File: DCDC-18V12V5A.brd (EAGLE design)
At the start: 40 x 24 mm, 38 parts, among them Q10 NMOSFET, Q9 NMOSFET, U1 LM3150MHX/NOPB

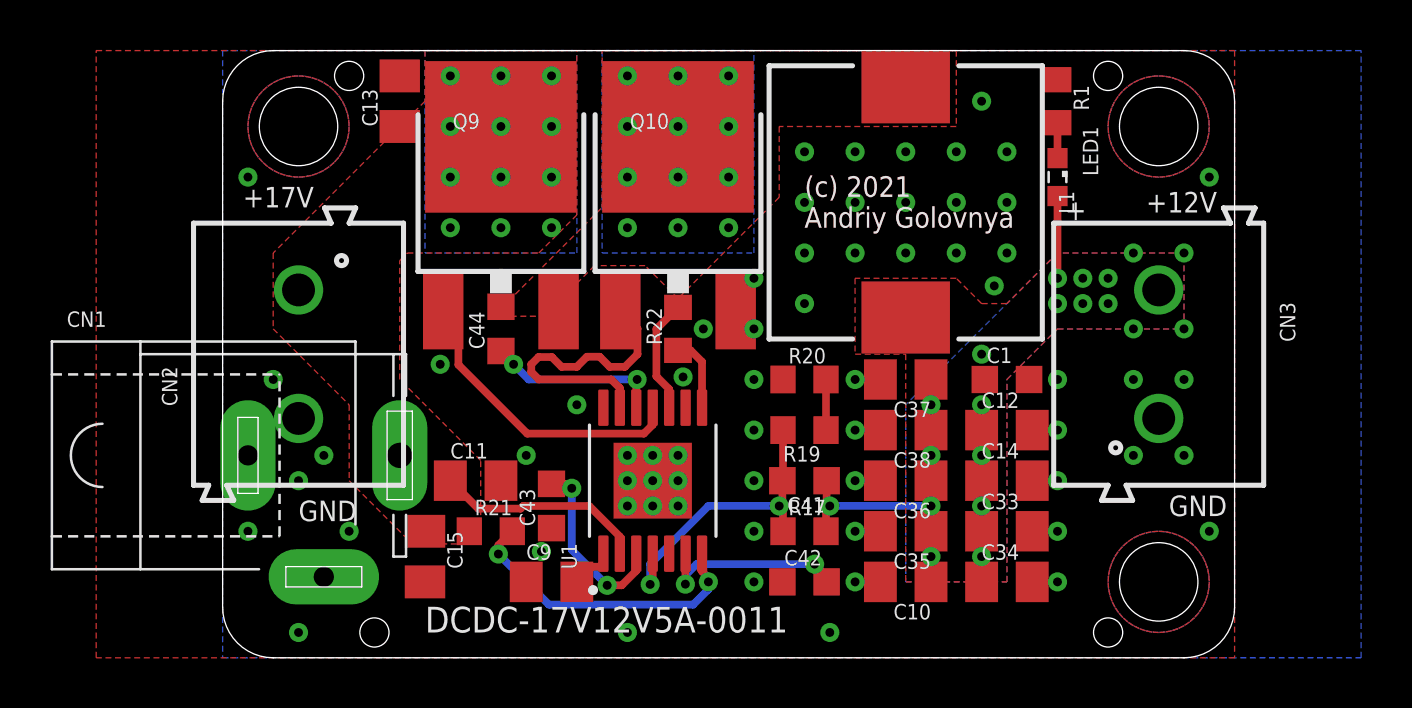
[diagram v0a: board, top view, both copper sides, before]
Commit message: Changed texts on 18V-12V boards. Generated CAM files. Generated PNG preview. Generated PDF schematics.
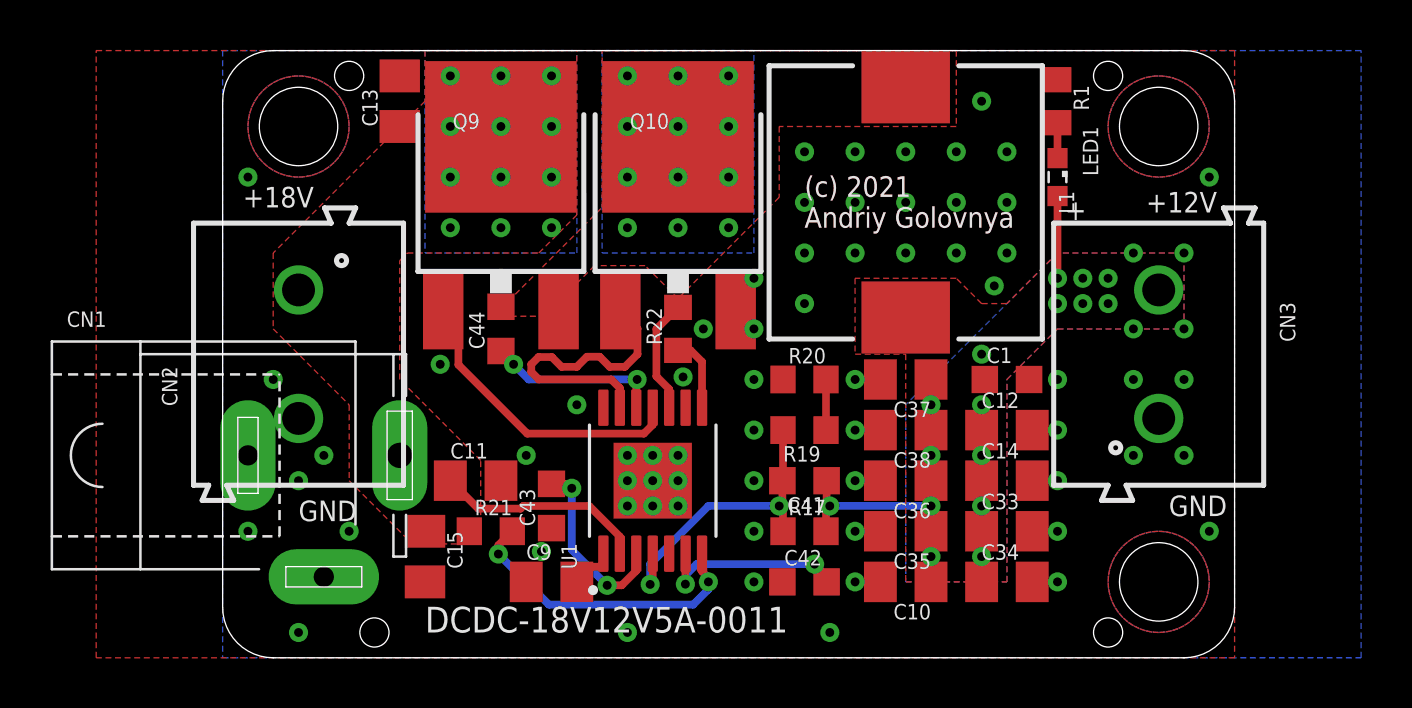
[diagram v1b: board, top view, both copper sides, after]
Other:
- board text added: "+18V"
- board text added: "DCDC-18V12V5A-0011"
- board text removed: "+17V"
- board text removed: "DCDC-17V12V5A-0011"
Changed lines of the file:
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@@
 <hole x="37" y="21" drill="3.1"/>
 <hole x="37" y="3" drill="3.1"/>
-<text x="33" y="20" size="1.6764" layer="22" font="vector" ratio="20" rot="MR0">DCDC-17V12V5A-0011</text>
-<text x="0.8" y="17.8" size="0.8128" layer="21" font="vector">+17V</text>
+<text x="33" y="20" size="1.6764" layer="22" font="vector" ratio="20" rot="MR0">DCDC-18V12V5A-0011</text>
+<text x="0.8" y="17.8" size="0.8128" layer="21" font="vector">+18V</text>
 <text x="3" y="5.4" size="0.8128" layer="21" font="vector">GND</text>
 <text x="37.4" y="5.6" size="0.8128" layer="21" font="vector">GND</text>
@@
 <text x="33" y="16" size="1.27" layer="22" font="vector" rot="MR0">(c) Andriy Golovnya</text>
 <text x="33" y="18" size="1.27" layer="22" font="vector" rot="MR0">12V/5A DC-DC Buck Converter</text>
-<text x="1.6" y="15.8" size="0.8128" layer="22" font="vector" rot="MR270">+17V</text>
+<text x="1.6" y="15.8" size="0.8128" layer="22" font="vector" rot="MR270">+18V</text>
 <text x="3.4" y="8.2" size="0.8128" layer="22" font="vector" rot="MR270">GND</text>
 <text x="39.3" y="15.8" size="0.8128" layer="22" font="vector" rot="MR270">+12V</text>
@@
 <text x="23" y="17" size="0.8128" layer="21" font="vector" ratio="20">(c) 2021
 Andriy Golovnya</text>
-<text x="8" y="1" size="1.016" layer="21" font="vector">DCDC-17V12V5A-0011</text>
+<text x="8" y="1" size="1.016" layer="21" font="vector">DCDC-18V12V5A-0011</text>
 </plain>
 <attributes>
